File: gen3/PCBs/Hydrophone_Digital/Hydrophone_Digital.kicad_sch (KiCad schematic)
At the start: 4 parts, among them J1 Conn_Coaxial, J2 Conn_Coaxial, J3 Conn_Coaxial, J4 Conn_Coaxial

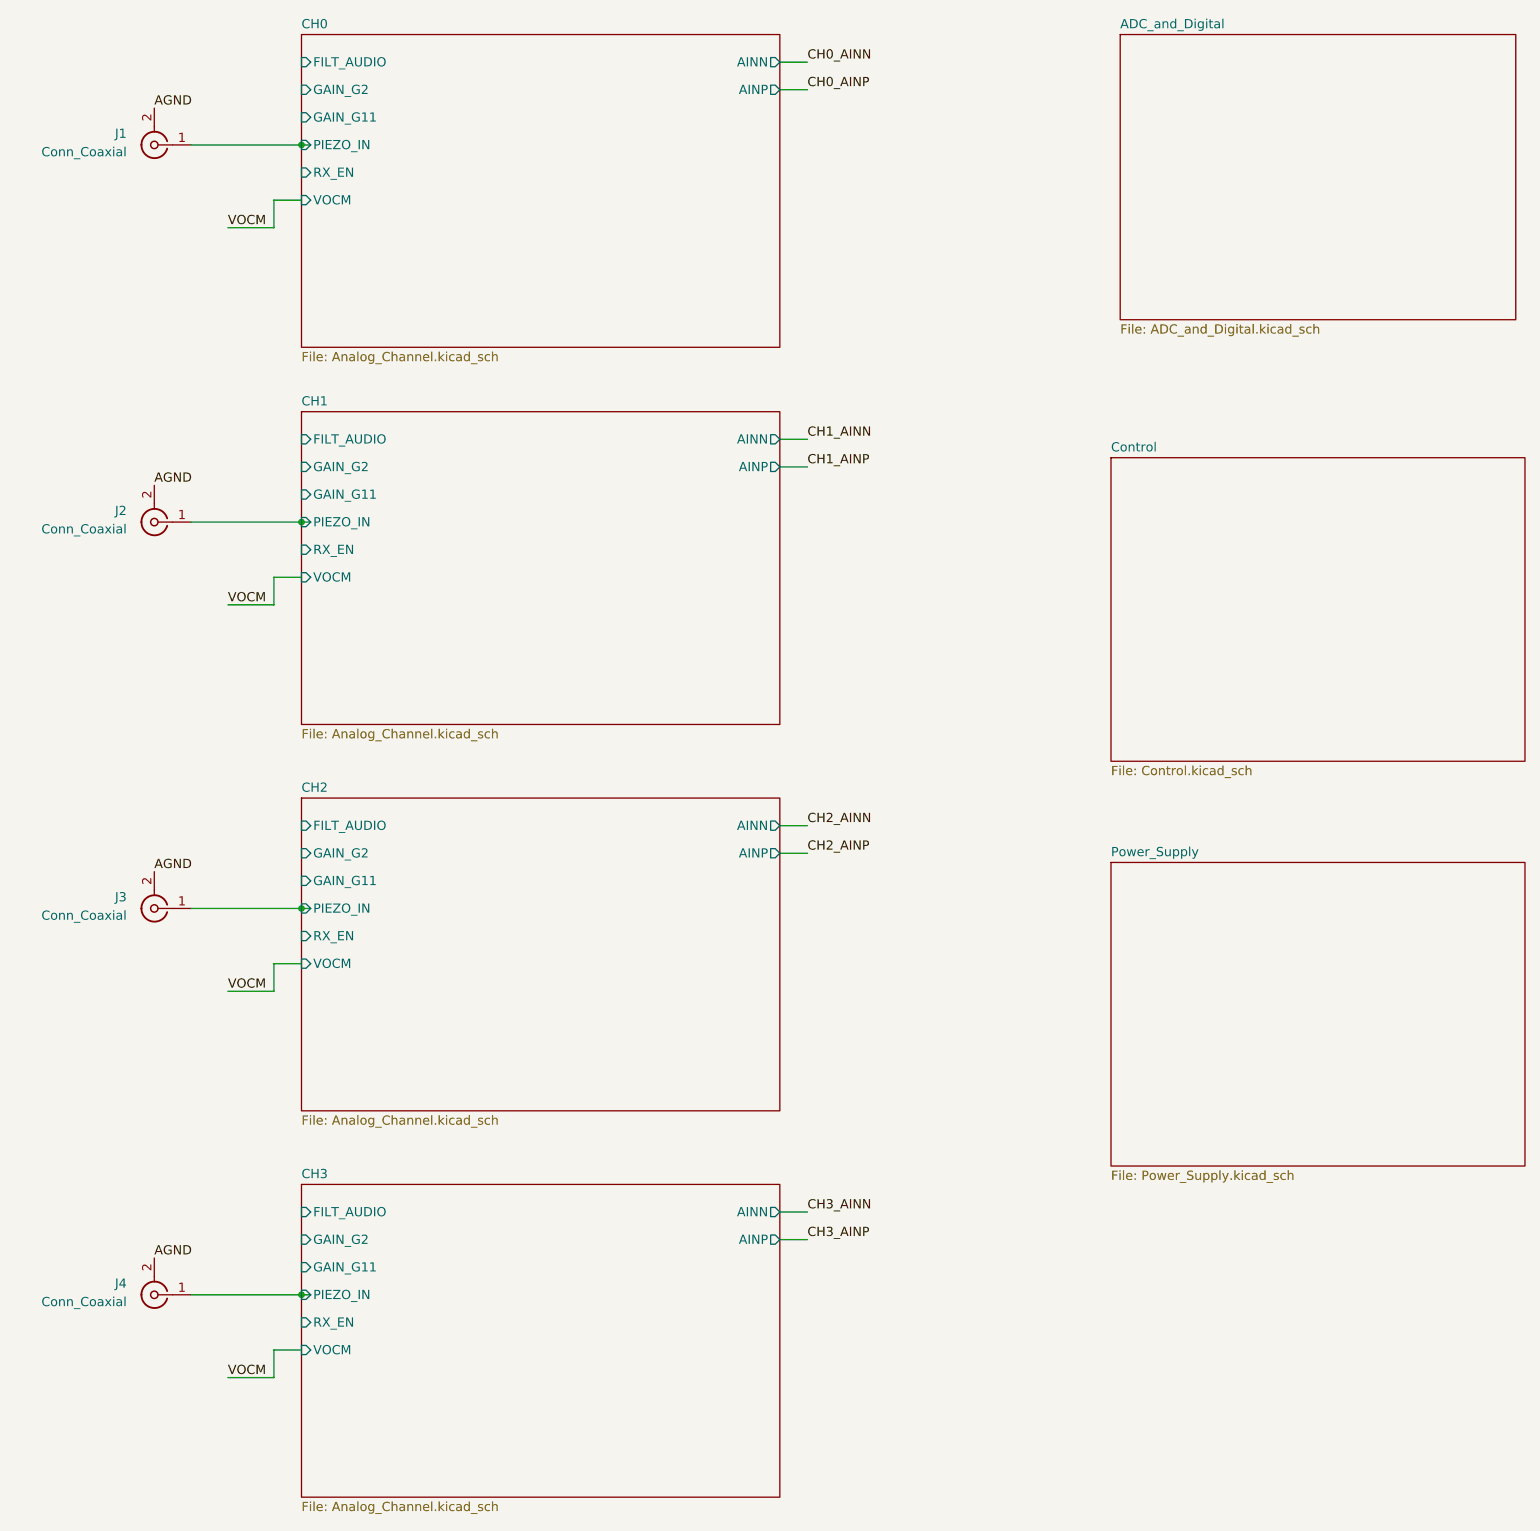
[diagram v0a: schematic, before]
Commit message: clean up digital root sheet - took out CH0-CH3 and power supply sheets, just ADC_and_Digital and Control left
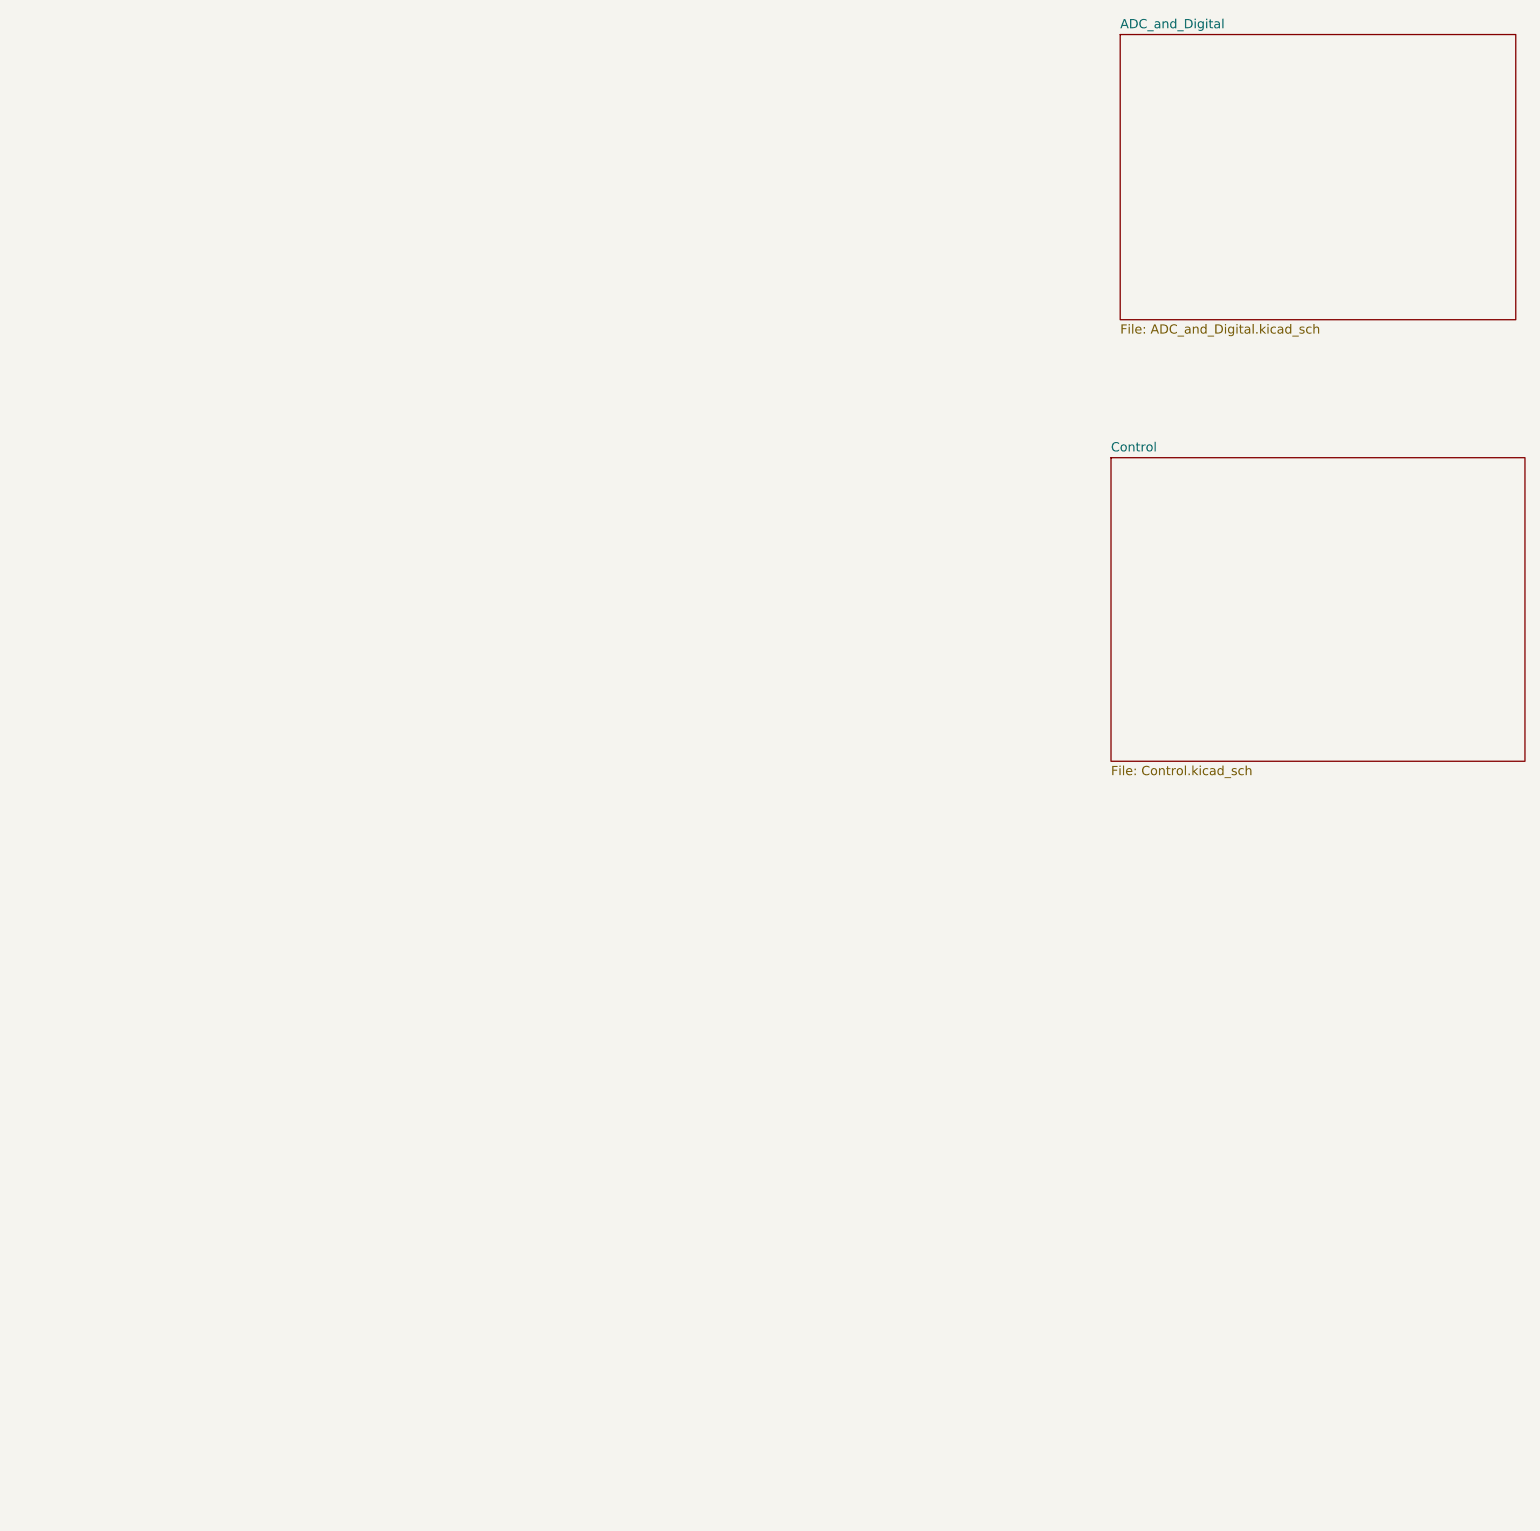
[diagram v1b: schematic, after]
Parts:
- removed J1, J2, J3, J4: Conn_Coaxial, symbol Connector:Conn_Coaxial
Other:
- removed sheet CH0
- removed sheet CH1
- removed sheet CH2
- removed sheet CH3
- removed sheet Power_Supply
